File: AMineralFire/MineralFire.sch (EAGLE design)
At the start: 55 parts, among them IC1 LM358, Q1 20MHz, T1 200mA/40V, U1 328P, U3 7805

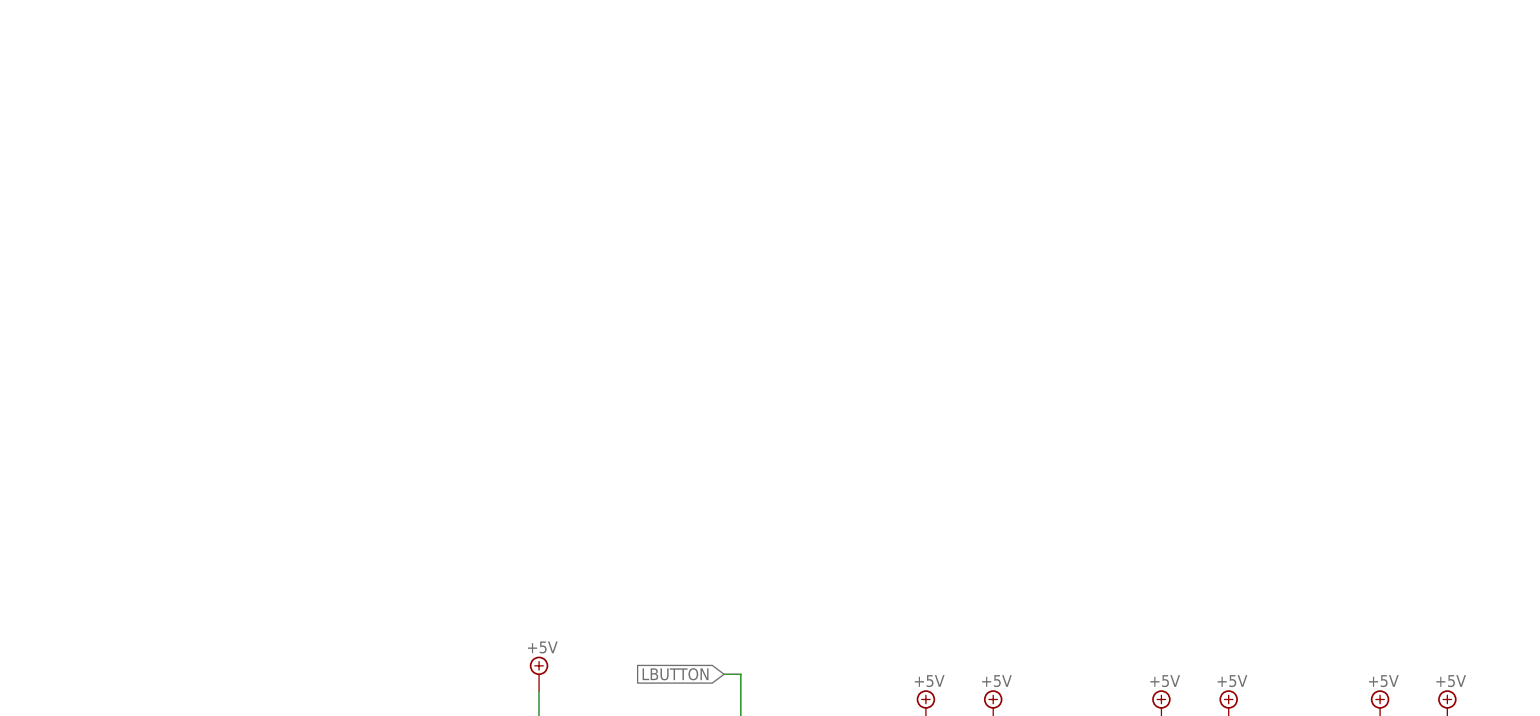
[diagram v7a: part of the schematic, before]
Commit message: Larger Board
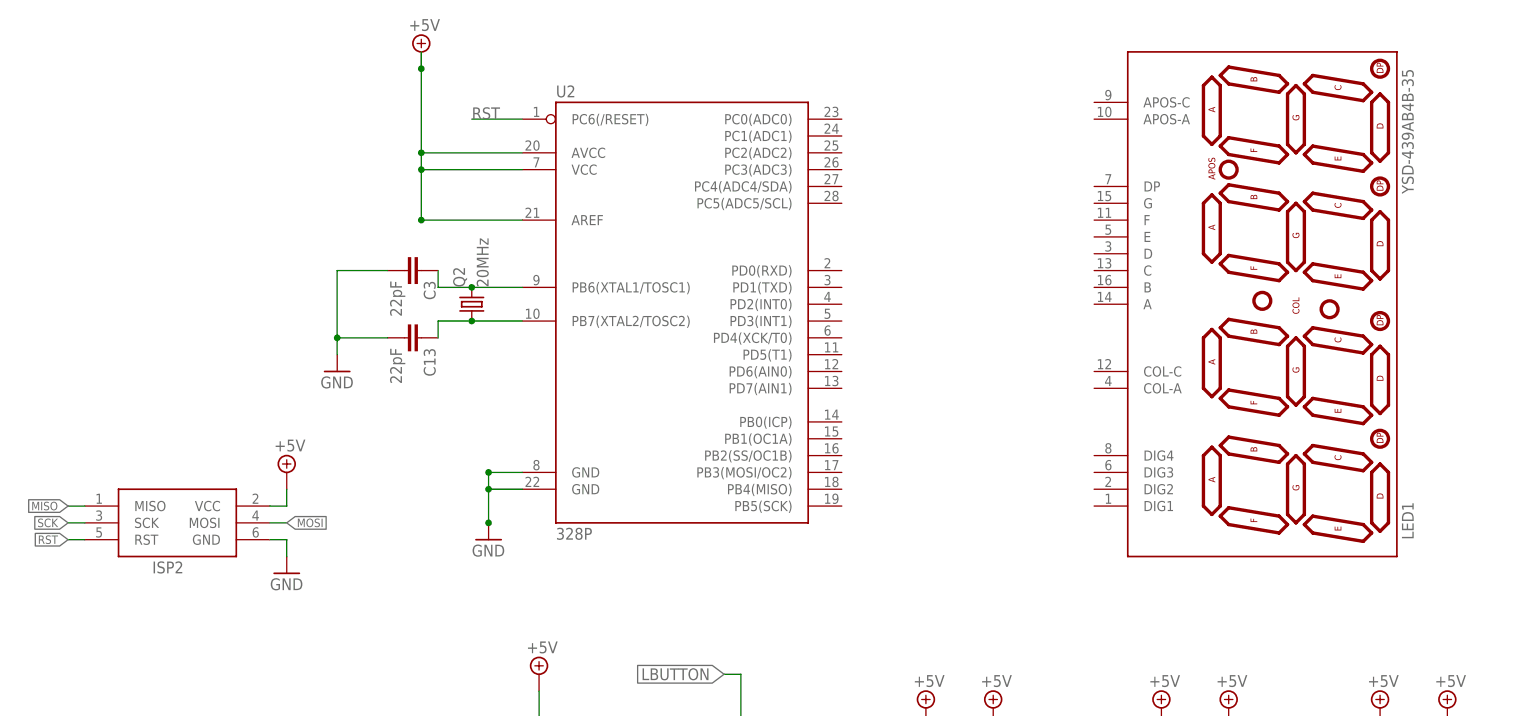
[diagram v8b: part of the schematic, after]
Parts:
- added C13, C3: 22pF, SparkFun-Capacitors:22PF-PTH-2.54MM-200V-5%
- added ISP2: AVRISP-6, adafruit:AVRISP-6
- added LED1: YSD-439AB4B-35, SparkFun-LED:7-SEGMENT-4DIGIT-10MM-BLUE
- added Q2: 20MHz, adafruit:CRYSTALHC49U70
- added U2: 328P, SparkFun-IC-Microcontroller:ATMEGA328P_PDIP
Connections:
- new net N$7: C3.1, Q2.2, U2.PB6(XTAL1/TOSC1)
- new net N$8: C13.1, Q2.1, U2.PB7(XTAL2/TOSC2)
- net +5V: now also ISP2.VCC, U2.AREF, U2.AVCC, U2.VCC
- net GND: now also C13.2, C3.2, ISP2.GND, U2.GND@1, U2.GND@2
- net MISO: now also ISP2.MISO
- net MOSI: now also ISP2.MOSI
- net RST: now also ISP2.RST, U2.PC6(/RESET)
- net SCK: now also ISP2.SCK
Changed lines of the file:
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@@
 <part name="SUPPLY29" library="supply2" deviceset="GND" device=""/>
 <part name="C6" library="rcl" deviceset="C-EU" device="075-032X103" value="100pf"/>
+<part name="Q2" library="adafruit" deviceset="CRYSTAL" device="HC49U70" value="20MHz"/>
+<part name="C3" library="SparkFun-Capacitors" deviceset="22PF" device="-PTH-2.54MM-200V-5%" value="22pF"/>
+<part name="C13" library="SparkFun-Capacitors" deviceset="22PF" device="-PTH-2.54MM-200V-5%" value="22pF"/>
+<part name="GND6" library="supply1" deviceset="GND" device=""/>
+<part name="U2" library="SparkFun-IC-Microcontroller" deviceset="ATMEGA328P_PDIP" device="" value="328P"/>
+<part name="GND7" library="supply1" deviceset="GND" device=""/>
+<part name="SUPPLY30" library="supply2" deviceset="+5V" device=""/>
+<part name="LED1" library="SparkFun-LED" deviceset="7-SEGMENT-4DIGIT-10MM" device="-BLUE" value="YSD-439AB4B-35"/>
+<part name="ISP2" library="adafruit" deviceset="AVRISP" device="-6"/>
+<part name="GND9" library="supply1" deviceset="GND" device=""/>
+<part name="SUPPLY31" library="supply2" deviceset="+5V" device=""/>
 </parts>
 <sheets>
@@
 <instance part="SUPPLY29" gate="GND" x="203.2" y="53.34"/>
 <instance part="C6" gate="G$1" x="271.78" y="48.26" rot="R90"/>
+<instance part="Q2" gate="G$1" x="50.8" y="205.74" rot="R90"/>
+<instance part="C3" gate="G$1" x="40.64" y="210.82" rot="R270"/>
+<instance part="C13" gate="G$1" x="40.64" y="200.66" rot="R270"/>
+<instance part="GND6" gate="1" x="30.48" y="195.58"/>
+<instance part="U2" gate="G$1" x="81.28" y="208.28"/>
+<instance part="GND7" gate="1" x="53.34" y="170.18"/>
+<instance part="SUPPLY30" gate="+5V" x="43.18" y="243.84"/>
+<instance part="LED1" gate="G$1" x="172.72" y="205.74" rot="R90"/>
+<instance part="ISP2" gate="G$1" x="5.08" y="172.72"/>
+<instance part="GND9" gate="1" x="22.86" y="165.1"/>
+<instance part="SUPPLY31" gate="+5V" x="22.86" y="180.34"/>
 </instances>
 <busses>
@@
 <pinref part="GND5" gate="1" pin="GND"/>
 </segment>
+<segment>
+<pinref part="C3" gate="G$1" pin="2"/>
+<wire x1="38.1" y1="210.82" x2="30.48" y2="210.82" width="0.1524" layer="91"/>
+<wire x1="30.48" y1="210.82" x2="30.48" y2="200.66" width="0.1524" layer="91"/>
+<pinref part="C13" gate="G$1" pin="2"/>
+<wire x1="30.48" y1="200.66" x2="38.1" y2="200.66" width="0.1524" layer="91"/>
+<wire x1="30.48" y1="200.66" x2="30.48" y2="198.12" width="0.1524" layer="91"/>
+<junction x="30.48" y="200.66"/>
+<pinref part="GND6" gate="1" pin="GND"/>
+</segment>
+<segment>
+<pinref part="U2" gate="G$1" pin="GND@1"/>
+<wire x1="58.42" y1="180.34" x2="53.34" y2="180.34" width="0.1524" layer="91"/>
+<pinref part="GND7" gate="1" pin="GND"/>
+<wire x1="53.34" y1="180.34" x2="53.34" y2="177.8" width="0.1524" layer="91"/>
+<pinref part="U2" gate="G$1" pin="GND@2"/>
+<wire x1="53.34" y1="172.72" x2="53.34" y2="177.8" width="0.1524" layer="91"/>
+<wire x1="53.34" y1="177.8" x2="58.42" y2="177.8" width="0.1524" layer="91"/>
+<junction x="53.34" y="177.8"/>
+<junction x="53.34" y="180.34"/>
+<junction x="53.34" y="172.72"/>
+</segment>
+<segment>
+<pinref part="ISP2" gate="G$1" pin="GND"/>
+<wire x1="20.32" y1="170.18" x2="22.86" y2="170.18" width="0.1524" layer="91"/>
+<wire x1="22.86" y1="170.18" x2="22.86" y2="167.64" width="0.1524" layer="91"/>
+<pinref part="GND9" gate="1" pin="GND"/>
+</segment>
 </net>
 <net name="RST" class="0">
@@
 <wire x1="63.5" y1="68.58" x2="55.88" y2="68.58" width="0.1524" layer="91"/>
 <label x="55.88" y="68.58" size="1.778" layer="95"/>
+</segment>
+<segment>
+<pinref part="U2" gate="G$1" pin="PC6(/RESET)"/>
+<wire x1="58.42" y1="233.68" x2="50.8" y2="233.68" width="0.1524" layer="91"/>
+<label x="50.8" y="233.68" size="1.778" layer="95"/>
+</segment>
+<segment>
+<pinref part="ISP2" gate="G$1" pin="RST"/>
+<wire x1="-7.62" y1="170.18" x2="-10.16" y2="170.18" width="0.1524" layer="91"/>
+<label x="-10.16" y="170.18" size="1.27" layer="95" rot="R180" xref="yes"/>
 </segment>
 </net>
@@
 <wire x1="60.96" y1="147.32" x2="60.96" y2="142.24" width="0.1524" layer="91"/>
 </segment>
+<segment>
+<pinref part="U2" gate="G$1" pin="AVCC"/>
+<wire x1="58.42" y1="228.6" x2="43.18" y2="228.6" width="0.1524" layer="91"/>
+<wire x1="43.18" y1="228.6" x2="43.18" y2="241.3" width="0.1524" layer="91"/>
+<pinref part="SUPPLY30" gate="+5V" pin="+5V"/>
+<wire x1="43.18" y1="241.3" x2="43.18" y2="243.84" width="0.1524" layer="91"/>
+<junction x="43.18" y="241.3"/>
+<junction x="43.18" y="228.6"/>
+<wire x1="43.18" y1="228.6" x2="43.18" y2="226.06" width="0.1524" layer="91"/>
+<pinref part="U2" gate="G$1" pin="VCC"/>
+<wire x1="43.18" y1="226.06" x2="58.42" y2="226.06" width="0.1524" layer="91"/>
+<wire x1="43.18" y1="226.06" x2="43.18" y2="218.44" width="0.1524" layer="91"/>
+<junction x="43.18" y="226.06"/>
+<pinref part="U2" gate="G$1" pin="AREF"/>
+<wire x1="43.18" y1="218.44" x2="58.42" y2="218.44" width="0.1524" layer="91"/>
+<junction x="43.18" y="218.44"/>
+</segment>
+<segment>
+<pinref part="ISP2" gate="G$1" pin="VCC"/>
+<wire x1="20.32" y1="175.26" x2="22.86" y2="175.26" width="0.1524" layer="91"/>
+<wire x1="22.86" y1="175.26" x2="22.86" y2="177.8" width="0.1524" layer="91"/>
+<pinref part="SUPPLY31" gate="+5V" pin="+5V"/>
+</segment>
 </net>
 <net name="MISO" class="0">
@@
 <pinref part="U1" gate="G$1" pin="PB4(MISO)"/>
 </segment>
+<segment>
+<pinref part="ISP2" gate="G$1" pin="MISO"/>
+<wire x1="-7.62" y1="175.26" x2="-10.16" y2="175.26" width="0.1524" layer="91"/>
+<label x="-10.16" y="175.26" size="1.27" layer="95" rot="R180" xref="yes"/>
+</segment>
 </net>
 <net name="SCK" class="0">
@@
 <label x="114.3" y="10.16" size="1.778" layer="95" xref="yes"/>
 </segment>
+<segment>
+<pinref part="ISP2" gate="G$1" pin="SCK"/>
+<wire x1="-7.62" y1="172.72" x2="-10.16" y2="172.72" width="0.1524" layer="91"/>
+<label x="-10.16" y="172.72" size="1.27" layer="95" rot="R180" xref="yes"/>
+</segment>
 </net>
 <net name="MOSI" class="0">
@@
 <label x="114.3" y="15.24" size="1.27" layer="95" xref="yes"/>
 <pinref part="U1" gate="G$1" pin="PB3(MOSI/OC2)"/>
+</segment>
+<segment>
+<pinref part="ISP2" gate="G$1" pin="MOSI"/>
+<wire x1="20.32" y1="172.72" x2="22.86" y2="172.72" width="0.1524" layer="91"/>
+<label x="22.86" y="172.72" size="1.27" layer="95" xref="yes"/>
 </segment>
 </net>
@@
 </segment>
 </net>
+<net name="N$7" class="0">
+<segment>
+<pinref part="Q2" gate="G$1" pin="2"/>
+<wire x1="58.42" y1="208.28" x2="50.8" y2="208.28" width="0.1524" layer="91"/>
+<wire x1="50.8" y1="208.28" x2="45.72" y2="208.28" width="0.1524" layer="91"/>
+<wire x1="45.72" y1="208.28" x2="45.72" y2="210.82" width="0.1524" layer="91"/>
+<junction x="50.8" y="208.28"/>
+<pinref part="C3" gate="G$1" pin="1"/>
+<pinref part="U2" gate="G$1" pin="PB6(XTAL1/TOSC1)"/>
+</segment>
+</net>
+<net name="N$8" class="0">
+<segment>
+<pinref part="Q2" gate="G$1" pin="1"/>
+<wire x1="58.42" y1="203.2" x2="50.8" y2="203.2" width="0.1524" layer="91"/>
+<wire x1="50.8" y1="203.2" x2="45.72" y2="203.2" width="0.1524" layer="91"/>
+<wire x1="45.72" y1="203.2" x2="45.72" y2="200.66" width="0.1524" layer="91"/>
+<junction x="50.8" y="203.2"/>
+<pinref part="C13" gate="G$1" pin="1"/>
+<pinref part="U2" gate="G$1" pin="PB7(XTAL2/TOSC2)"/>
+</segment>
+</net>
